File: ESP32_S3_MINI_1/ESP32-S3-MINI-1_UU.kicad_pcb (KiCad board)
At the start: 2 copper layers, 20.3 x 45.7 mm, 54 parts, among them IC1 TPS6282533DMQR, IC2 BQ25185DLHR, J1 JST_2mm_LiPo, J2 USB4120-03-C, J3 Qwiic_Vertical, J4 Castellated_1x01, J7 Castellated_1x01, J8 Castellated_1x16, J9 Castellated_1x18, U1 LM66100DCK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

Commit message: Trace cleanup
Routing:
- net GND: track 63.1 -> 72.7 mm
- added copper zone on F.Cu, net Net-(IC1-SW)

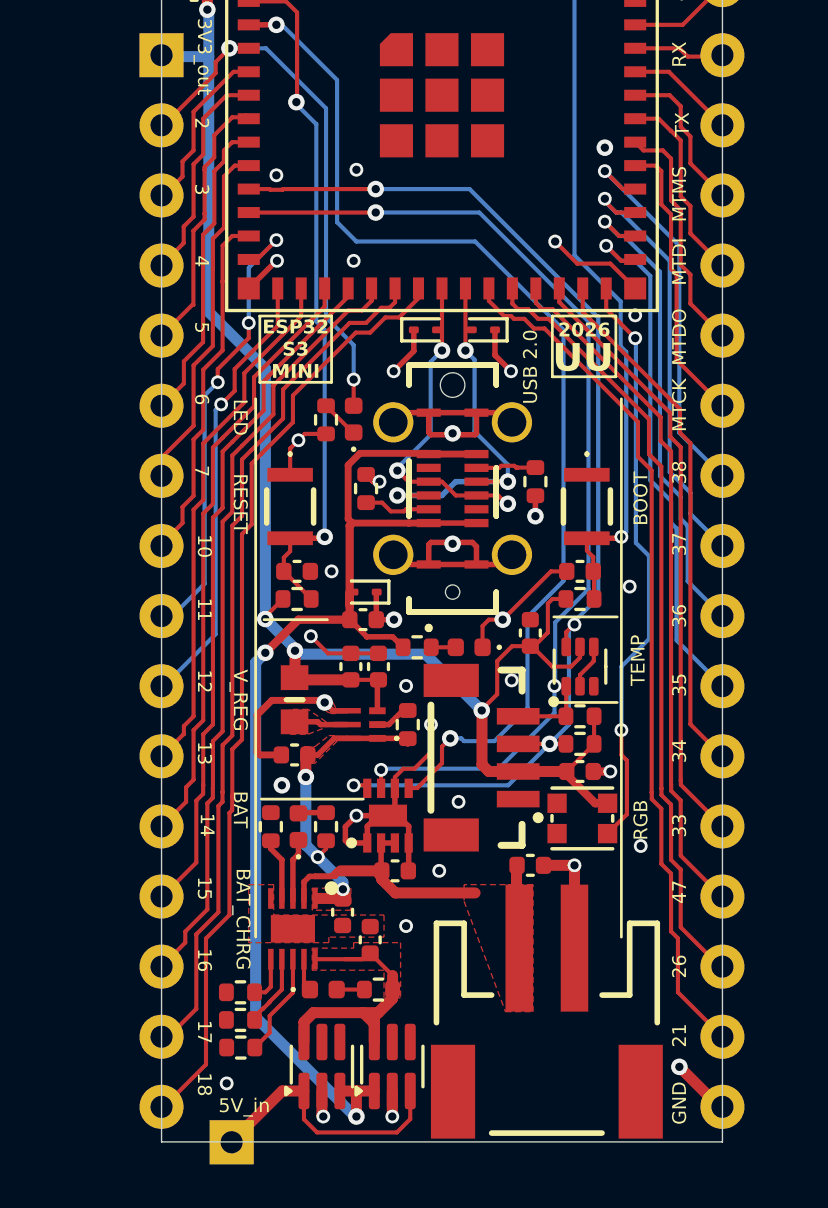
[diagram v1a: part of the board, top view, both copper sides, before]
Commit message: Differential USB routing
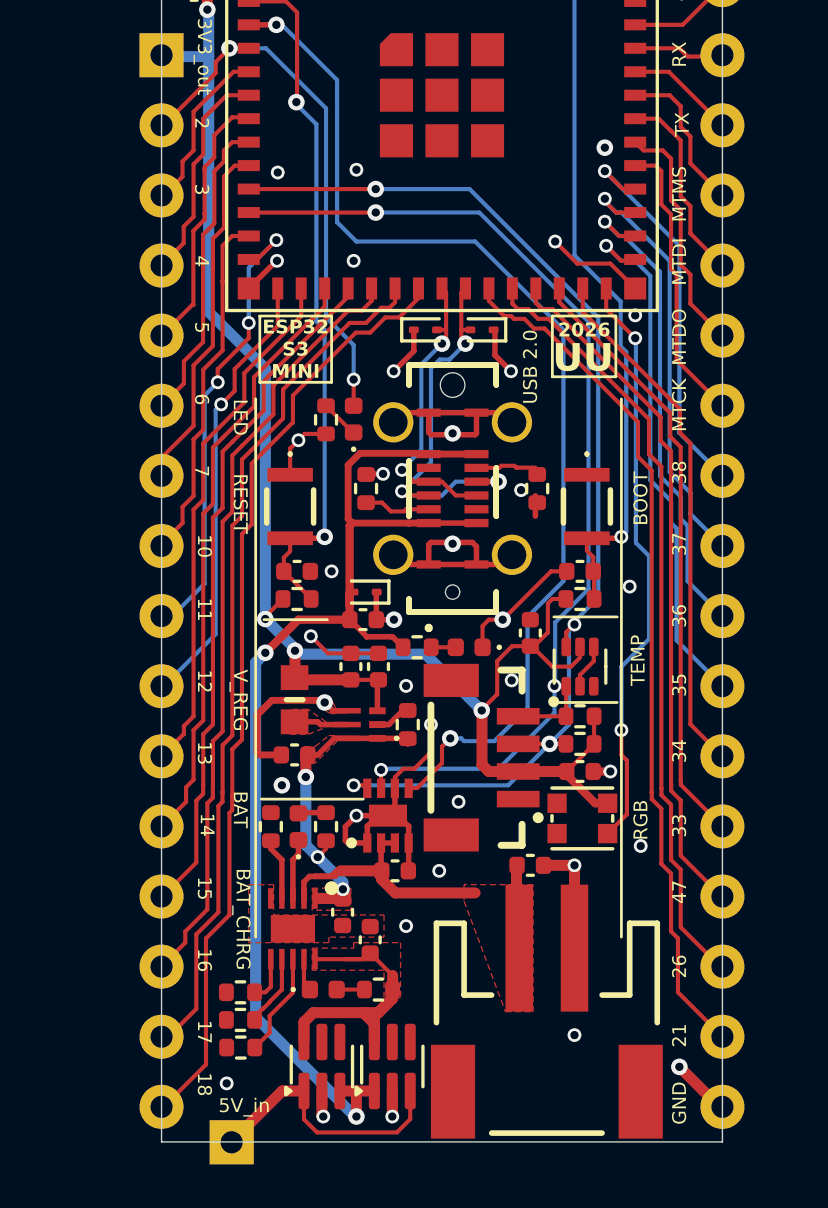
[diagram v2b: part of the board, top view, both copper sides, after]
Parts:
- moved R4 0.26 mm to (185.8, 135.1)
- moved D7 0.05 mm to (183.8, 129.3)
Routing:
- net D-: track 11.8 -> 10.7 mm, vias 3 -> 2
- net GND: vias 37 -> 38
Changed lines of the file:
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@@
 	(footprint "Diode_SMD:D_SOD-923"
 		(layer "F.Cu")
-		(at 183.9 129.3 180)
+		(at 183.85 129.3 180)
 		(descr "https://www.onsemi.com/pub/Collateral/ESD9B-D.PDF#page=4")
 		(tags "Diode SOD923")
@@
 	(footprint "PCM_SparkFun-Resistor:R_0402_1005Metric"
 		(layer "F.Cu")
-		(at 185.785 134.8 -90)
+		(at 185.85 135.05 -90)
 		(descr "Resistor SMD 0402 (1005 Metric), square (rectangular) end terminal, IPC_7351 nominal, (Body size source: IPC-SM-782 page 72, https://www.pcb-3d.com/wordpress/wp-content/uploads/ipc-sm-782a_amendment_1_and_2.pdf), generated with kicad-footprint-generator")
 		(tags "SparkFun resistor")
@@
 	)
 	(segment
+		(start 179.672231 134.517769)
+		(end 179.65 134.54)
+		(width 0.15)
+		(layer "F.Cu")
+		(net 1)
+	)
+	(segment
 		(start 178.15 142.8)
 		(end 178.074 142.724)
@@
 	)
 	(segment
-		(start 180.136 134.8)
-		(end 179.91 134.8)
-		(width 0.2)
-		(layer "F.Cu")
-		(net 1)
-	)
-	(segment
 		(start 177.43 133.07)
 		(end 178.2 133.07)
@@
 	)
 	(segment
+		(start 180.264711 134.517769)
+		(end 179.672231 134.517769)
+		(width 0.2)
+		(layer "F.Cu")
+		(net 1)
+	)
+	(segment
 		(start 183.5 137)
 		(end 182.835 137)
@@
 	)
 	(segment
-		(start 179.91 134.8)
-		(end 179.65 134.54)
-		(width 0.2)
-		(layer "F.Cu")
-		(net 1)
-	)
-	(segment
 		(start 182 137)
 		(end 182.735 137)
@@
 	)
 	(via
-		(at 185.785 136.05)
-		(size 0.6)
+		(at 185.265857 135.106111)
+		(size 0.5)
 		(drill 0.3)
 		(layers "F.Cu" "B.Cu")
@@
 	)
 	(via
+		(at 187.2 154.85)
+		(size 0.5)
+		(drill 0.3)
+		(layers "F.Cu" "B.Cu")
+		(free yes)
+		(net 1)
+	)
+	(via
 		(at 189.6 148)
 		(size 0.5)
@@
 	)
 	(via
-		(at 180.136 134.8)
+		(at 180.264711 134.517769)
 		(size 0.5)
 		(drill 0.3)
@@
 	)
 	(via
-		(at 176.4 123.7)
+		(at 176.45 123.6)
 		(size 0.5)
 		(drill 0.3)
@@
 	)
 	(segment
-		(start 176.617877 124.226)
-		(end 176.182123 124.226)
+		(start 187.17651 139.974949)
+		(end 186.9 140.251459)
 		(width 0.15)
 		(layer "F.Cu")
@@
 	)
 	(segment
-		(start 187.17651 139.974949)
-		(end 186.9 140.251459)
+		(start 180 124.2)
+		(end 175.4 124.2)
 		(width 0.15)
 		(layer "F.Cu")
@@
 	)
 	(segment
-		(start 176.182123 124.226)
-		(end 176.156123 124.2)
-		(width 0.15)
-		(layer "F.Cu")
-		(net 31)
-	)
-	(segment
 		(start 179.2 145.8)
 		(end 179.584 145.8)
@@
 	)
 	(segment
-		(start 180 124.2)
-		(end 176.643877 124.2)
-		(width 0.15)
-		(layer "F.Cu")
-		(net 31)
-	)
-	(segment
 		(start 186.9 140.251459)
 		(end 186.9 140.7875)
@@
 	)
 	(segment
-		(start 176.156123 124.2)
-		(end 175.4 124.2)
-		(width 0.15)
-		(layer "F.Cu")
-		(net 31)
-	)
-	(segment
-		(start 176.643877 124.2)
-		(end 176.617877 124.226)
-		(width 0.15)
-		(layer "F.Cu")
-		(net 31)
-	)
-	(segment
 		(start 179.584 145.8)
 		(end 179.694 145.91)
@@
 	)
 	(segment
-		(start 183.65 134.8)
-		(end 184.785 134.8)
+		(start 184.45 134.8)
+		(end 183.65 134.8)
+		(width 0.2)
+		(layer "F.Cu")
+		(net 32)
+	)
+	(segment
+		(start 183.1 129.3)
+		(end 183.1 129.65)
+		(width 0.15)
+		(layer "F.Cu")
+		(net 32)
+	)
+	(segment
+		(start 183.25 127.8)
+		(end 183.1 127.95)
+		(width 0.15)
+		(layer "F.Cu")
+		(net 32)
+	)
+	(segment
+		(start 183.1 129.65)
+		(end 183.25 129.8)
+		(width 0.15)
+		(layer "F.Cu")
+		(net 32)
+	)
+	(segment
+		(start 183.43 129.3)
+		(end 183.1 129.3)
 		(width 0.15)
 		(layer "F.Cu")
@@
 	(segment
 		(start 181.92 135.3)
-		(end 180.785 135.3)
+		(end 181.1 135.3)
 		(width 0.15)
 		(layer "F.Cu")
@@
 	)
 	(segment
-		(start 183.25 130.2)
-		(end 183.25 127.8)
+		(start 181.1 135.3)
+		(end 180.95 135.15)
+		(width 0.15)
+		(layer "F.Cu")
+		(net 32)
+	)
+	(segment
+		(start 183.1 127.95)
+		(end 183.1 129.3)
 		(width 0.15)
 		(layer "F.Cu")
@@
 	)
 	(via
-		(at 184.785 134.8)
+		(at 184.45 134.8)
 		(size 0.6)
 		(drill 0.3)
@@
 	)
 	(via
-		(at 183.25 130.05)
+		(at 183.25 129.8)
 		(size 0.6)
 		(drill 0.3)
@@
 	)
 	(via
-		(at 180.785 135.3)
-		(size 0.6)
+		(at 180.95 135.15)
+		(size 0.5)
 		(drill 0.3)
 		(layers "F.Cu" "B.Cu")
@@
 	)
 	(segment
-		(start 183.581 132.981)
-		(end 183.581 130.381)
+		(start 182.4 135.3)
+		(end 181.1 135.3)
 		(width 0.15)
 		(layer "B.Cu")
@@
 	)
 	(segment
-		(start 184.785 134.8)
-		(end 184.785 134.185)
+		(start 182.001 134.099)
+		(end 180.95 135.15)
 		(width 0.15)
 		(layer "B.Cu")
@@
 	)
 	(segment
-		(start 184.785 134.185)
-		(end 183.581 132.981)
+		(start 183.25 129.8)
+		(end 182.674 130.376)
 		(width 0.15)
 		(layer "B.Cu")
@@
 	(segment
 		(start 182.9 134.8)
-		(end 184.785 134.8)
-		(width 0.2)
+		(end 184.45 134.8)
+		(width 0.15)
+		(layer "B.Cu")
+		(net 32)
+	)
+	(segment
+		(start 182.674 130.376)
+		(end 182.320388 130.376)
+		(width 0.15)
 		(layer "B.Cu")
 		(net 32)
@@
 		(start 182.4 135.3)
 		(end 182.9 134.8)
-		(width 0.2)
+		(width 0.15)
 		(layer "B.Cu")
 		(net 32)
 	)
 	(segment
-		(start 183.581 130.381)
-		(end 183.25 130.05)
+		(start 182.001 130.695388)
+		(end 182.001 134.099)
 		(width 0.15)
 		(layer "B.Cu")
@@
 	)
 	(segment
-		(start 180.785 135.3)
-		(end 182.4 135.3)
-		(width 0.2)
+		(start 181.1 135.3)
+		(end 180.95 135.15)
+		(width 0.15)
+		(layer "B.Cu")
+		(net 32)
+	)
+	(segment
+		(start 182.320388 130.376)
+		(end 182.001 130.695388)
+		(width 0.15)
 		(layer "B.Cu")
 		(net 32)
@@
 	)
 	(segment
-		(start 181.185 134.8)
-		(end 180.785 134.4)
+		(start 182.55 129.3)
+		(end 182.55 129.65)
 		(width 0.15)
 		(layer "F.Cu")
@@
 	)
 	(segment
-		(start 184.435057 135.3)
-		(end 184.735057 135.6)
+		(start 181.92 134.8)
+		(end 181.375 134.8)
 		(width 0.15)
 		(layer "F.Cu")
@@
 	)
 	(segment
-		(start 184.735057 135.6)
-		(end 184.785 135.6)
-		(width 0.2)
+		(start 182.22 129.3)
+		(end 182.55 129.3)
+		(width 0.15)
 		(layer "F.Cu")
 		(net 43)
 	)
 	(segment
-		(start 181.92 134.8)
-		(end 182.4 134.8)
+		(start 182.55 127.95)
+		(end 182.55 129.3)
 		(width 0.15)
 		(layer "F.Cu")
@@
 	)
 	(segment
-		(start 183.65 135.3)
-		(end 184.435057 135.3)
+		(start 181.92 134.8)
+		(end 182.4 134.8)
 		(width 0.15)
 		(layer "F.Cu")
@@
 	)
 	(segment
-		(start 181.92 134.8)
-		(end 181.185 134.8)
+		(start 182.55 129.65)
+		(end 182.4 129.8)
 		(width 0.15)
 		(layer "F.Cu")
@@
 	)
 	(segment
-		(start 182.9 135.3)
-		(end 183.65 135.3)
+		(start 181.375 134.8)
+		(end 180.95 134.375)
 		(width 0.15)
 		(layer "F.Cu")
@@
 	)
 	(segment
-		(start 182.4 130.05)
-		(end 182.4 127.8)
+		(start 182.9 135.3)
+		(end 183.65 135.3)
 		(width 0.15)
 		(layer "F.Cu")
@@
 		(net 43)
 	)
-	(via
-		(at 184.785 135.6)
-		(size 0.6)
-		(drill 0.3)
-		(layers "F.Cu" "B.Cu")
+	(segment
+		(start 182.4 127.8)
+		(end 182.55 127.95)
+		(width 0.15)
+		(layer "F.Cu")
 		(net 43)
 	)
 	(via
-		(at 182.4 130.05)
+		(at 182.4 129.8)
 		(size 0.6)
 		(drill 0.3)
@@
 	)
 	(via
-		(at 180.785 134.4)
-		(size 0.6)
+		(at 180.95 134.375)
+		(size 0.5)
 		(drill 0.3)
 		(layers "F.Cu" "B.Cu")
@@
 	)
 	(segment
-		(start 181.989 130.461)
-		(end 182.4 130.05)
+		(start 180.95 134.375)
+		(end 180.95 134.35)
 		(width 0.15)
 		(layer "B.Cu")
@@
 	)
 	(segment
-		(start 181.989 133.096)
-		(end 181.989 130.461)
+		(start 181.65 133.65)
+		(end 181.65 130.55)
 		(width 0.15)
 		(layer "B.Cu")
@@
 	)
 	(segment
-		(start 180.785 134.3)
-		(end 181.989 133.096)
+		(start 182.4 129.8)
+		(end 181.65 130.55)
 		(width 0.15)
 		(layer "B.Cu")
@@
 	)
 	(segment
-		(start 180.785 134.4)
-		(end 180.785 134.3)
-		(width 0.2)
+		(start 180.95 134.35)
+		(end 181.65 133.65)
+		(width 0.15)
 		(layer "B.Cu")
 		(net 43)

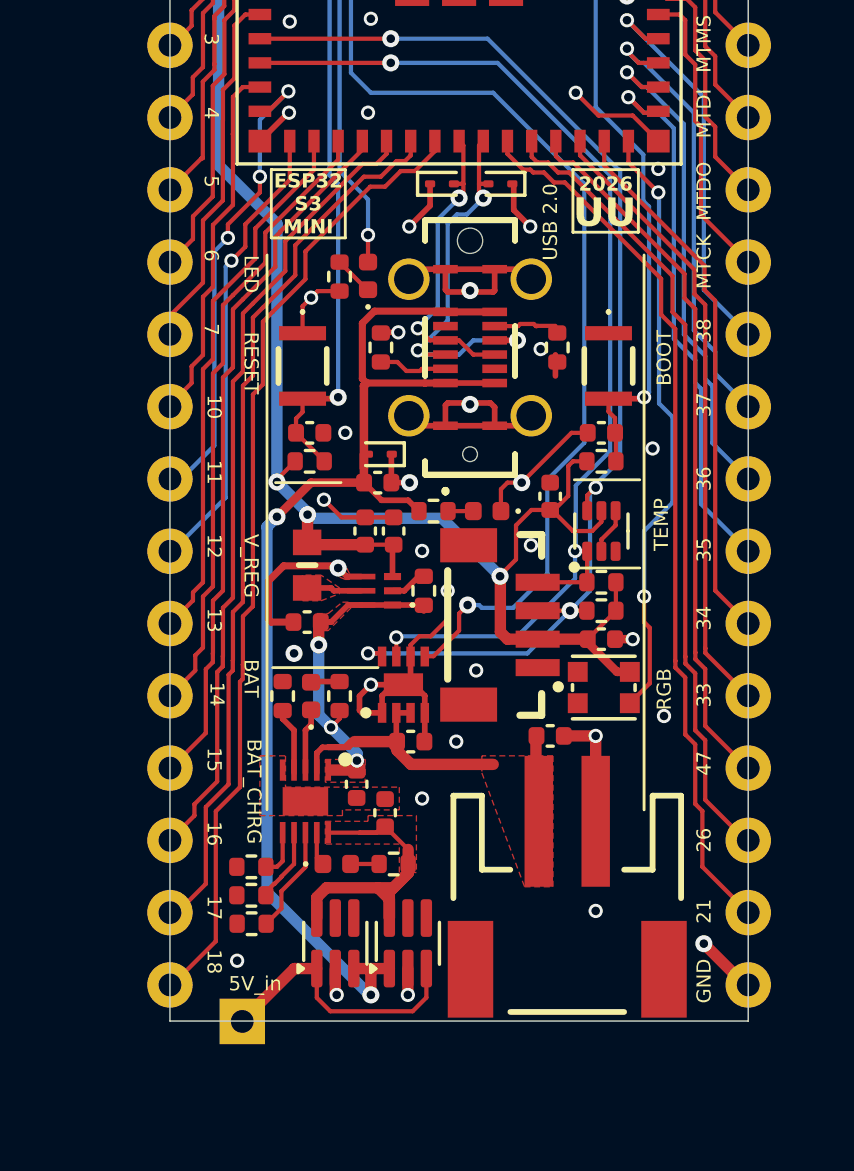
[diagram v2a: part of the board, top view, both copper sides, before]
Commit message: Update ESP32 PCB projects and generated assets
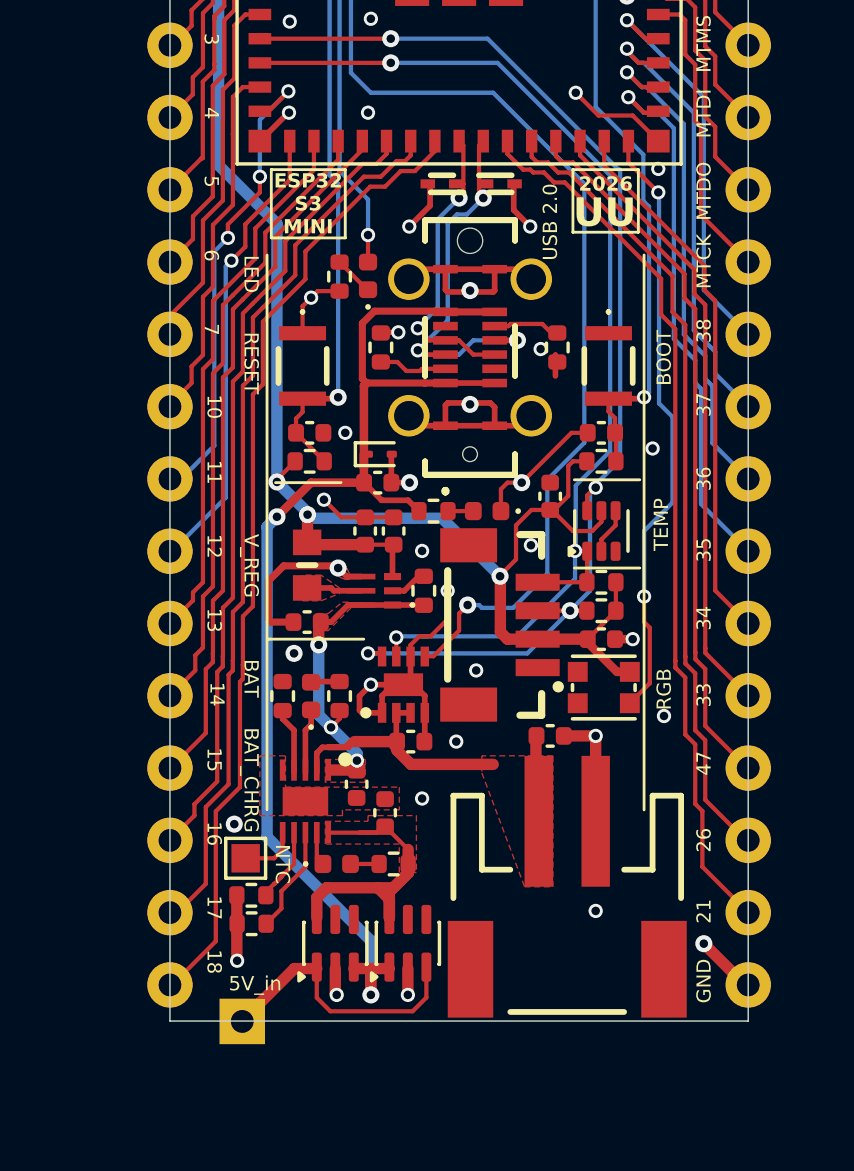
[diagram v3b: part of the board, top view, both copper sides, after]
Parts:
- removed TH1: 10k, PCM_SparkFun-Resistor:R_0402_1005Metric
- added TP3: TestPoint, ESP32-S3-MINI-1_Components:TestPoint_Pad_1.0x1.0mm, F.Cu at (174.9, 153.0)
- C4: footprint PCM_SparkFun-Capacitor:C_0402_1005Metric -> Capacitor_SMD:C_0402_1005Metric
- D7, D8: footprint Diode_SMD:D_SOD-923 -> ESP32-S3-MINI-1_Components:SODFL1006X40N
- IC1: footprint ESP32:TPS6282533DMQR -> ESP32-S3-MINI-1_Components:TPS6282533DMQR
- IC2: footprint ESP32:SON40P220X200X80-11N -> ESP32-S3-MINI-1_Components:SON40P220X200X80-11N
- J2: footprint ESP32:USB412003C -> ESP32-S3-MINI-1_Components:USB412003C
- J4, J7: footprint ESP32:Castellated_1x01_P2.54mm_D0.80mm -> Castellated_Connectors:Castellated_1x01_P2.54mm_D0.80mm
- L1: footprint ESP32:INDC1608X75N -> ESP32-S3-MINI-1_Components:INDC1608X75N
- S1, S2: footprint ESP32:NANOT160AS -> ESP32-S3-MINI-1_Components:NANOT160AS
- U4: value TMP102 -> TMP112A; footprint PCM_SparkFun-Semiconductor-Standard:SOT-563 -> Package_TO_SOT_SMD:SOT-563
- turned D1 to 0 degrees
- turned D7 to 0 degrees
- turned D8 to 180 degrees
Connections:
- D1 pad 1: GND -> V_USB
- D1 pad 2: V_USB -> GND
- D7 pad 1: GND -> D+
- D7 pad 2: D+ -> GND
- D8 pad 1: GND -> D-
- D8 pad 2: D- -> GND
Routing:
- net GND: track 72.7 -> 75.0 mm, vias 38 -> 39
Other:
- board text added: "NTC"
